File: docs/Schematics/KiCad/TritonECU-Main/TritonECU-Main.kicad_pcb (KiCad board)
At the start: 4 copper layers, 158 x 174 mm, 4 parts, among them J1 EEC-V 104

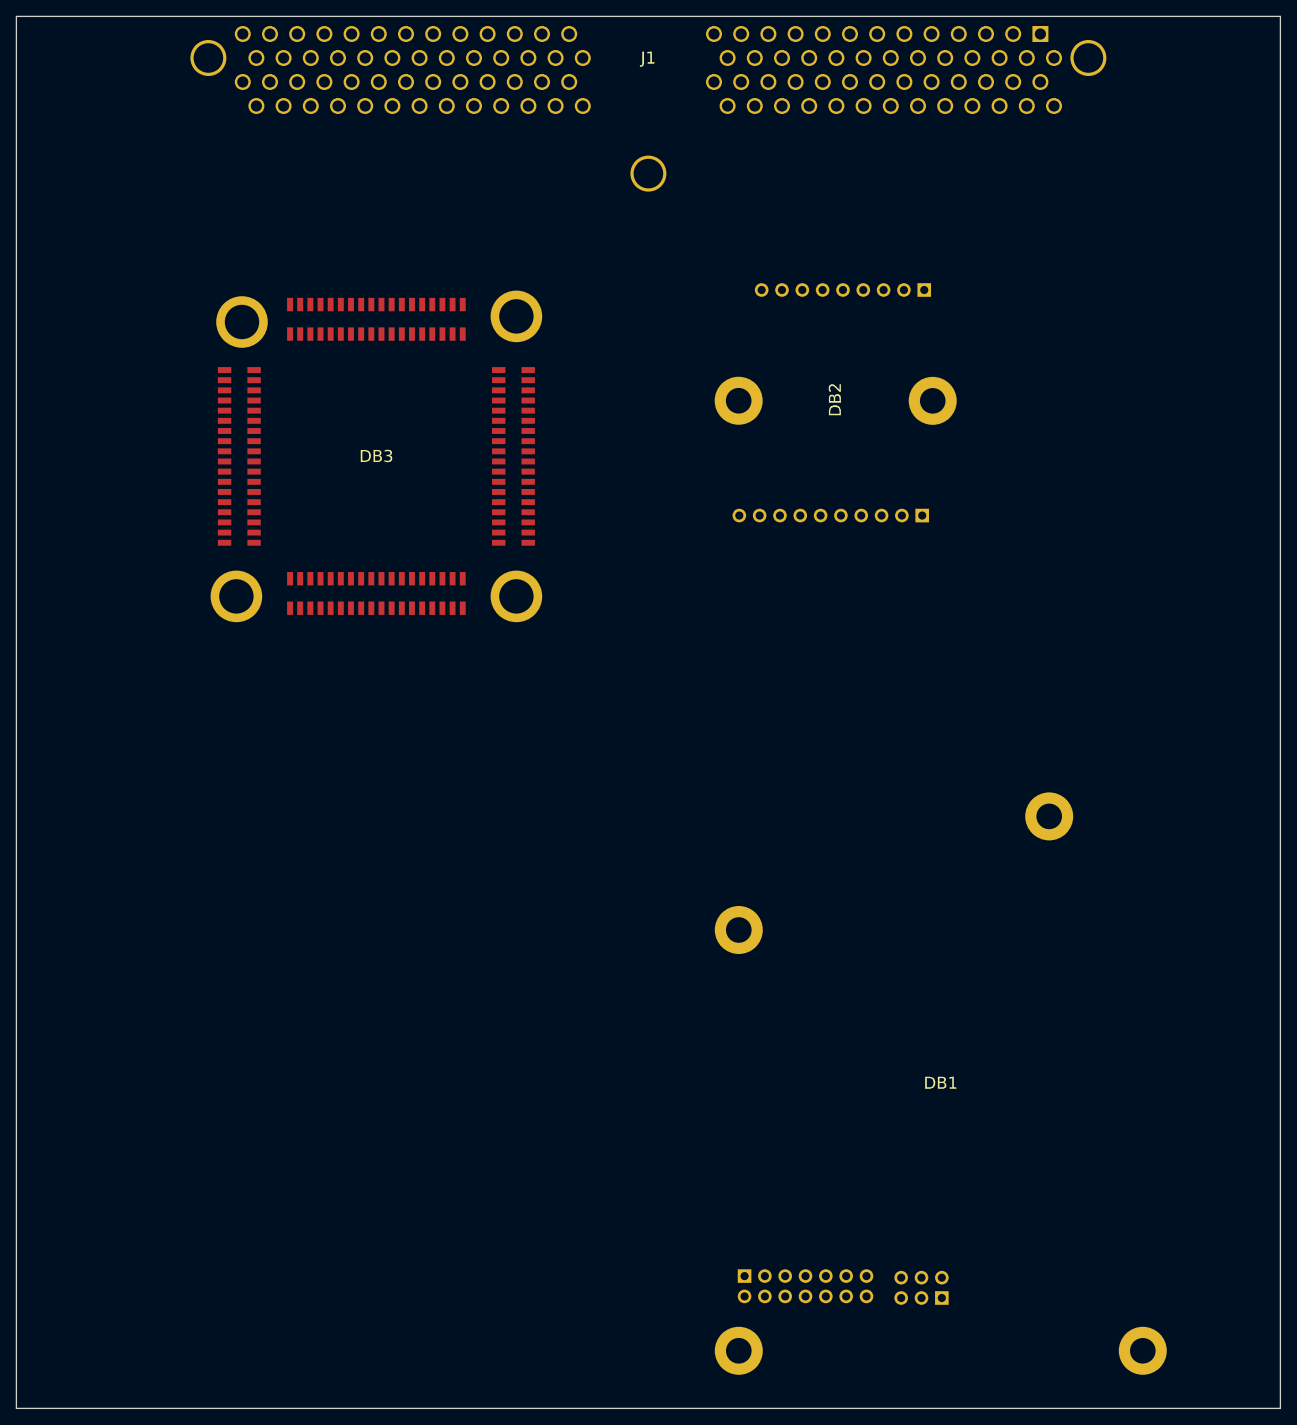
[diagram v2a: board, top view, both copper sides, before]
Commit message: Carrier: ignition, injection and rails sheets, placed on the main board
- eecv_pins.py: the EEC-V connector map for the 5.4L, checked. Corrects SSA/SSB
  to pins 6/11: Ford's "PCM 27 (*6)" legend is * = 5.4L, and 27/1 are coils 5/6
  on this truck (schematic-ecu-v1.txt and measurements-wanted.md fixed).
- carrier_pinmap.py: adds TCS (O/D cancel, pin 29) on PE1, polled; 4x4-low has
  no PCM pin in either source, marked [CONFIRM]. 100 signals, 5 spare.
- Interconnect sheet rebuilt every run with every connector and module pin
  labelled from the two maps (symbol UUIDs kept); deliberate no-connects flagged.
- gen_carrier.py: Rails, Ignition (74HCT541, 8x ISL9V3040, TPS3823A-33 watchdog
  on NRST and OE2 via BSS138, JP101 v1 strap) and Injection (8x ZXMS6005DGQ,
  10k input pulldowns). Deterministic symbol UUIDs keep the PCB linked. Own
  symbols for the IntelliFET (the Samacsys import is broken) and NCV8772.
- gen_carrier_pcb.py: adds missing parts to the board linked to their symbols,
  sets every pad net from the netlist, places a first-draft floor plan by
  connector position. DRC: no courtyard overlaps, schematic parity clean.
- ADC goes back on the carrier: adc-daughterboard.md superseded.

Co-Authored-By: Claude Opus 5.5 <noreply@anthropic.com>
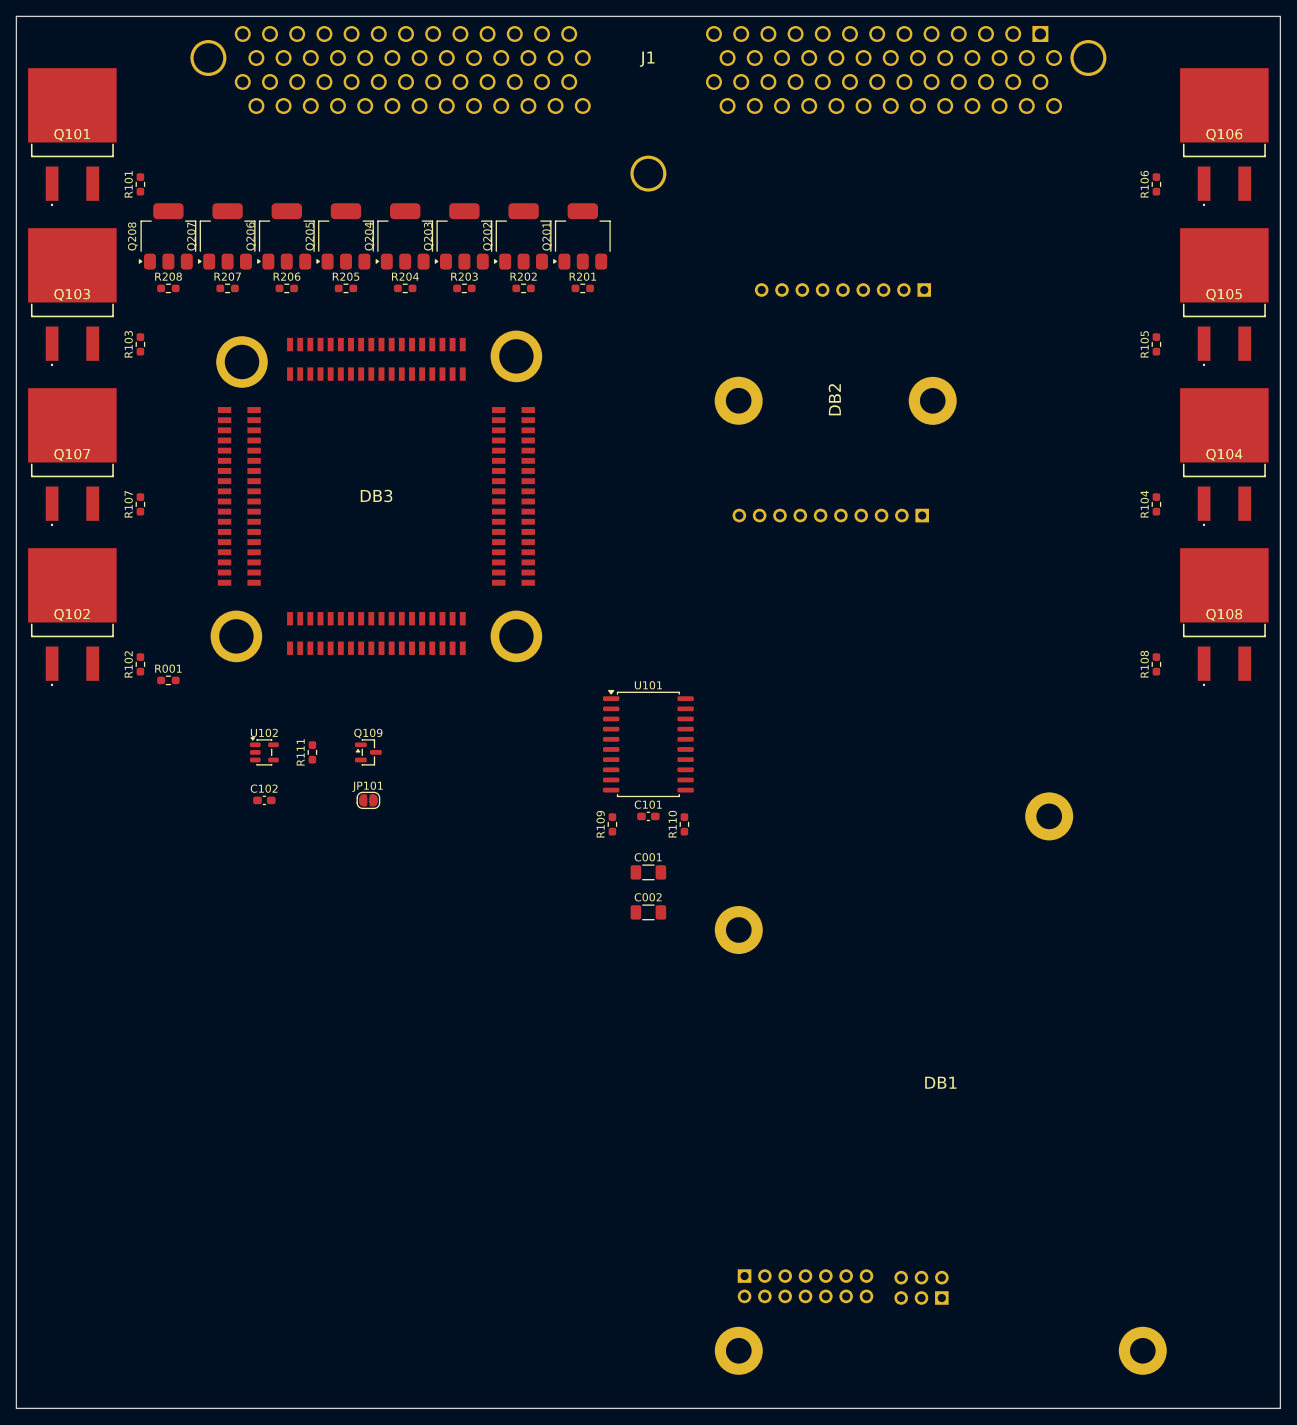
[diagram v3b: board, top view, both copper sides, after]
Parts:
- added C001: 10u, Capacitor_SMD:C_1206_3216Metric_Pad1.33x1.80mm_HandSolder, F.Cu at (104.0, 132.0)
- added C002: 10u, Capacitor_SMD:C_1206_3216Metric_Pad1.33x1.80mm_HandSolder, F.Cu at (104.0, 137.0)
- added C101: 100n, Capacitor_SMD:C_0603_1608Metric_Pad1.08x0.95mm_HandSolder, F.Cu at (104.0, 125.0)
- added C102: 100n, Capacitor_SMD:C_0603_1608Metric_Pad1.08x0.95mm_HandSolder, F.Cu at (56.0, 123.0)
- added JP101: OE2 strap, Jumper:SolderJumper-2_P1.3mm_Open_RoundedPad1.0x1.5mm, F.Cu at (69.0, 123.0)
- added Q101: ISL9V3040S3ST, Samacsys:ISL9V3040S3ST, F.Cu at (32.0, 38.0)
- added Q102: ISL9V3040S3ST, Samacsys:ISL9V3040S3ST, F.Cu at (32.0, 98.0)
- added Q103: ISL9V3040S3ST, Samacsys:ISL9V3040S3ST, F.Cu at (32.0, 58.0)
- added Q104: ISL9V3040S3ST, Samacsys:ISL9V3040S3ST, F.Cu at (176.0, 78.0)
- added Q105: ISL9V3040S3ST, Samacsys:ISL9V3040S3ST, F.Cu at (176.0, 58.0)
- added Q106: ISL9V3040S3ST, Samacsys:ISL9V3040S3ST, F.Cu at (176.0, 38.0)
- added Q107: ISL9V3040S3ST, Samacsys:ISL9V3040S3ST, F.Cu at (32.0, 78.0)
- added Q108: ISL9V3040S3ST, Samacsys:ISL9V3040S3ST, F.Cu at (176.0, 98.0)
- added Q109: BSS138, Package_TO_SOT_SMD:SOT-23, F.Cu at (69.0, 117.0)
- added Q201: ZXMS6005DGQTA, Package_TO_SOT_SMD:SOT-223-3_TabPin2, F.Cu at (95.8, 52.5)
- added Q202: ZXMS6005DGQTA, Package_TO_SOT_SMD:SOT-223-3_TabPin2, F.Cu at (88.4, 52.5)
- added Q203: ZXMS6005DGQTA, Package_TO_SOT_SMD:SOT-223-3_TabPin2, F.Cu at (81.0, 52.5)
- added Q204: ZXMS6005DGQTA, Package_TO_SOT_SMD:SOT-223-3_TabPin2, F.Cu at (73.6, 52.5)
- added Q205: ZXMS6005DGQTA, Package_TO_SOT_SMD:SOT-223-3_TabPin2, F.Cu at (66.2, 52.5)
- added Q206: ZXMS6005DGQTA, Package_TO_SOT_SMD:SOT-223-3_TabPin2, F.Cu at (58.8, 52.5)
- added Q207: ZXMS6005DGQTA, Package_TO_SOT_SMD:SOT-223-3_TabPin2, F.Cu at (51.4, 52.5)
- added Q208: ZXMS6005DGQTA, Package_TO_SOT_SMD:SOT-223-3_TabPin2, F.Cu at (44.0, 52.5)
- added R001: 0, Resistor_SMD:R_0603_1608Metric_Pad0.98x0.95mm_HandSolder, F.Cu at (44.0, 108.0)
- added R101: 470, Resistor_SMD:R_0603_1608Metric_Pad0.98x0.95mm_HandSolder, F.Cu at (40.5, 46.0)
- added R102: 470, Resistor_SMD:R_0603_1608Metric_Pad0.98x0.95mm_HandSolder, F.Cu at (40.5, 106.0)
- added R103: 470, Resistor_SMD:R_0603_1608Metric_Pad0.98x0.95mm_HandSolder, F.Cu at (40.5, 66.0)
- added R104: 470, Resistor_SMD:R_0603_1608Metric_Pad0.98x0.95mm_HandSolder, F.Cu at (167.5, 86.0)
- added R105: 470, Resistor_SMD:R_0603_1608Metric_Pad0.98x0.95mm_HandSolder, F.Cu at (167.5, 66.0)
- added R106: 470, Resistor_SMD:R_0603_1608Metric_Pad0.98x0.95mm_HandSolder, F.Cu at (167.5, 46.0)
- added R107: 470, Resistor_SMD:R_0603_1608Metric_Pad0.98x0.95mm_HandSolder, F.Cu at (40.5, 86.0)
- added R108: 470, Resistor_SMD:R_0603_1608Metric_Pad0.98x0.95mm_HandSolder, F.Cu at (167.5, 106.0)
- added R109: 10k, Resistor_SMD:R_0603_1608Metric_Pad0.98x0.95mm_HandSolder, F.Cu at (99.5, 126.0)
- added R110: 10k, Resistor_SMD:R_0603_1608Metric_Pad0.98x0.95mm_HandSolder, F.Cu at (108.5, 126.0)
- added R111: 1M, Resistor_SMD:R_0603_1608Metric_Pad0.98x0.95mm_HandSolder, F.Cu at (62.0, 117.0)
- added R201: 10k, Resistor_SMD:R_0603_1608Metric_Pad0.98x0.95mm_HandSolder, F.Cu at (95.8, 59.0)
- added R202: 10k, Resistor_SMD:R_0603_1608Metric_Pad0.98x0.95mm_HandSolder, F.Cu at (88.4, 59.0)
- added R203: 10k, Resistor_SMD:R_0603_1608Metric_Pad0.98x0.95mm_HandSolder, F.Cu at (81.0, 59.0)
- added R204: 10k, Resistor_SMD:R_0603_1608Metric_Pad0.98x0.95mm_HandSolder, F.Cu at (73.6, 59.0)
- added R205: 10k, Resistor_SMD:R_0603_1608Metric_Pad0.98x0.95mm_HandSolder, F.Cu at (66.2, 59.0)
- added R206: 10k, Resistor_SMD:R_0603_1608Metric_Pad0.98x0.95mm_HandSolder, F.Cu at (58.8, 59.0)
- added R207: 10k, Resistor_SMD:R_0603_1608Metric_Pad0.98x0.95mm_HandSolder, F.Cu at (51.4, 59.0)
- added R208: 10k, Resistor_SMD:R_0603_1608Metric_Pad0.98x0.95mm_HandSolder, F.Cu at (44.0, 59.0)
- added U101: 74HCT541, Package_SO:SOIC-20W_7.5x12.8mm_P1.27mm, F.Cu at (104.0, 116.0)
- added U102: TPS3823A-33DBVR, Package_TO_SOT_SMD:SOT-23-5, F.Cu at (56.0, 117.0)
- moved DB3 5.00 mm to (70.0, 85.0)
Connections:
- DB1 pad A10: SDA -> I2C_SDA
- DB1 pad A12: 3.3_ENOUT -> ENOUT
- DB1 pad A6: SCL -> I2C_SCL
- DB1 pad A9: 3_GOOD -> unconnected-(DB1-3_GOOD-PadA9)
- DB1 pad B1: +5V -> GND
- DB1 pad B3: +VIN -> VPWR
- DB1 pad B4: +VIN -> VPWR
- DB3 pad A10: unconnected-(DB3-PC13-PadA10) -> IGN_WAKE
- DB3 pad A11: unconnected-(DB3-PF0-PadA11) -> I2C_SDA
- DB3 pad A12: unconnected-(DB3-PF1-PadA12) -> I2C_SCL
- DB3 pad A13: unconnected-(DB3-PF2-PadA13) -> U_SHDN
- DB3 pad A14: unconnected-(DB3-PF3-PadA14) -> DPFE
- DB3 pad A15: unconnected-(DB3-PF4-PadA15) -> TFT
- DB3 pad A16: unconnected-(DB3-PF5-PadA16) -> VIN_ALERT
- DB3 pad A19: unconnected-(DB3-PF6-PadA19) -> O2_DN1
- DB3 pad A20: unconnected-(DB3-PF7-PadA20) -> O2_DN2
- DB3 pad A21: unconnected-(DB3-PF8-PadA21) -> IAC
- DB3 pad A22: unconnected-(DB3-PF9-PadA22) -> VREF_FAULT
- DB3 pad A23: unconnected-(DB3-PF10-PadA23) -> FP_MON
- DB3 pad A24: unconnected-(DB3-NRST-PadA24) -> NRST
- DB3 pad A25: unconnected-(DB3-PC0-PadA25) -> TR3A
- DB3 pad A26: unconnected-(DB3-PC1-PadA26) -> VREF_CS
- DB3 pad A27: unconnected-(DB3-PC2-PadA27) -> VREF_STB
- DB3 pad A28: unconnected-(DB3-PC3-PadA28) -> KNOCK
- DB3 pad A31: unconnected-(DB3-PA0-PadA31) -> CAN_RX_WAKE
- DB3 pad A32: unconnected-(DB3-PA1-PadA32) -> J1850_RX
- DB3 pad A33: unconnected-(DB3-PA2-PadA33) -> MUX_OUT
- DB3 pad A4: unconnected-(DB3-PE2-PadA4) -> ENOUT
- DB3 pad A5: unconnected-(DB3-PE3-PadA5) -> M_SYNC
- DB3 pad A6: unconnected-(DB3-PE4-PadA6) -> FLT
- DB3 pad A7: unconnected-(DB3-PE5-PadA7) -> EVAP
- DB3 pad A8: unconnected-(DB3-PE6-PadA8) -> EGR
- DB3 pad A9: unconnected-(DB3-VBAT-PadA9) -> VBAT
- DB3 pad B10: unconnected-(DB3-PC5-PadB10) -> VREF_SEL
- DB3 pad B11: unconnected-(DB3-PB0-PadB11) -> MUX_S0
- DB3 pad B12: unconnected-(DB3-PB1-PadB12) -> MUX_S1
- DB3 pad B13: unconnected-(DB3-PB2-PadB13) -> VREF_EN
- DB3 pad B14: unconnected-(DB3-PF11-PadB14) -> TR1
- DB3 pad B15: unconnected-(DB3-PF12-PadB15) -> TR2
- DB3 pad B18: unconnected-(DB3-PF13-PadB18) -> VREF_IN1
- DB3 pad B19: unconnected-(DB3-PF14-PadB19) -> TR4
- DB3 pad B2: unconnected-(DB3-PA3-PadB2) -> VSS_OUT
- DB3 pad B20: unconnected-(DB3-PF15-PadB20) -> BRAKE
- DB3 pad B21: unconnected-(DB3-PG0-PadB21) -> ACC
- DB3 pad B22: unconnected-(DB3-PG1-PadB22) -> 5_GOOD
- DB3 pad B23: unconnected-(DB3-PE7-PadB23) -> FPUMP
- DB3 pad B24: unconnected-(DB3-PE8-PadB24) -> 4X4L
- DB3 pad B25: unconnected-(DB3-PE9-PadB25) -> INJ1
- DB3 pad B28: unconnected-(DB3-PE10-PadB28) -> ACP
- DB3 pad B29: unconnected-(DB3-PE11-PadB29) -> INJ2
- DB3 pad B30: unconnected-(DB3-PE12-PadB30) -> FAN1
- DB3 pad B31: unconnected-(DB3-PE13-PadB31) -> INJ3
- DB3 pad B32: unconnected-(DB3-PE14-PadB32) -> INJ4
- DB3 pad B33: unconnected-(DB3-PE15-PadB33) -> FAN2
- DB3 pad B34: unconnected-(DB3-PB10-PadB34) -> CMP
- DB3 pad B35: unconnected-(DB3-PB11-PadB35) -> ADC_CONVST
- DB3 pad B5: unconnected-(DB3-PA4-PadB5) -> O2_BIAS
- DB3 pad B6: unconnected-(DB3-PA5-PadB6) -> TACH
- DB3 pad B7: unconnected-(DB3-PA6-PadB7) -> SPEED
- DB3 pad B8: unconnected-(DB3-PA7-PadB8) -> MUX_S2
- DB3 pad B9: unconnected-(DB3-PC4-PadB9) -> VREF_IN2
- DB3 pad C10: unconnected-(DB3-PD12-PadC10) -> COIL1
- DB3 pad C11: unconnected-(DB3-PD13-PadC11) -> COIL2
- DB3 pad C14: unconnected-(DB3-PD14-PadC14) -> COIL3
- DB3 pad C15: unconnected-(DB3-PD15-PadC15) -> COIL4
- DB3 pad C16: unconnected-(DB3-PG2-PadC16) -> HTR11
- DB3 pad C17: unconnected-(DB3-PG3-PadC17) -> HTR21
- DB3 pad C18: unconnected-(DB3-PG4-PadC18) -> HTR12
- DB3 pad C19: unconnected-(DB3-PG5-PadC19) -> HTR22
- DB3 pad C2: unconnected-(DB3-PB12-PadC2) -> SSB
- DB3 pad C20: unconnected-(DB3-PG6-PadC20) -> VENT
- DB3 pad C21: unconnected-(DB3-PG7-PadC21) -> IMCC
- DB3 pad C22: unconnected-(DB3-PG8-PadC22) -> SSA
- DB3 pad C25: unconnected-(DB3-PC6-PadC25) -> COIL5
- DB3 pad C26: unconnected-(DB3-PC7-PadC26) -> COIL6
- DB3 pad C27: unconnected-(DB3-PC8-PadC27) -> COIL7
- DB3 pad C28: unconnected-(DB3-PC9-PadC28) -> COIL8
- DB3 pad C29: unconnected-(DB3-PA8-PadC29) -> PWM_OE
- DB3 pad C3: unconnected-(DB3-PB13-PadC3) -> CCS
- DB3 pad C30: unconnected-(DB3-PA9-PadC30) -> USB_VBUS
- DB3 pad C32: unconnected-(DB3-PA11-PadC32) -> USB_DM
- DB3 pad C33: unconnected-(DB3-PA12-PadC33) -> USB_DP
- DB3 pad C4: unconnected-(DB3-PB14-PadC4) -> INJ7
- DB3 pad C5: unconnected-(DB3-PB15-PadC5) -> INJ8
- DB3 pad C8: unconnected-(DB3-PD10-PadC8) -> WDI
- DB3 pad C9: unconnected-(DB3-PD11-PadC9) -> COIL_ARM
- DB3 pad D10: unconnected-(DB3-PD3-PadD10) -> ADC_BUSY
- DB3 pad D11: unconnected-(DB3-PD4-PadD11) -> ADC_RESET
- DB3 pad D12: unconnected-(DB3-PD5-PadD12) -> CAN_STB
- DB3 pad D15: unconnected-(DB3-PD6-PadD15) -> SD_CK
- DB3 pad D16: unconnected-(DB3-PD7-PadD16) -> SD_CMD
- DB3 pad D17: unconnected-(DB3-PG9-PadD17) -> SD_D0
- DB3 pad D21: unconnected-(DB3-PG13-PadD21) -> J1850_TXP
- DB3 pad D22: unconnected-(DB3-PG14-PadD22) -> J1850_TXN
- DB3 pad D25: unconnected-(DB3-PG15-PadD25) -> J1850_NSLEEP
- DB3 pad D27: unconnected-(DB3-PB4-PadD27) -> INJ5
- DB3 pad D28: unconnected-(DB3-PB5-PadD28) -> INJ6
- DB3 pad D29: unconnected-(DB3-PB6-PadD29) -> OSS
- DB3 pad D3: unconnected-(DB3-PA15-PadD3) -> CKP
- DB3 pad D30: unconnected-(DB3-PB7-PadD30) -> TSS
- DB3 pad D31: unconnected-(DB3-BOOT0-PadD31) -> BOOT0
- DB3 pad D32: unconnected-(DB3-PB8-PadD32) -> EPC
- DB3 pad D33: unconnected-(DB3-PB9-PadD33) -> TCC
- DB3 pad D34: unconnected-(DB3-PE0-PadD34) -> TC_SPEED
- DB3 pad D35: unconnected-(DB3-PE1-PadD35) -> TCS
- DB3 pad D4: unconnected-(DB3-PC10-PadD4) -> ADC_SCK
- DB3 pad D5: unconnected-(DB3-PC11-PadD5) -> ADC_MISO
- DB3 pad D7: unconnected-(DB3-PD0-PadD7) -> CAN_RX
- DB3 pad D8: unconnected-(DB3-PD1-PadD8) -> CAN_TX
- DB3 pad D9: unconnected-(DB3-PD2-PadD9) -> ADC_CS
- J1 pad 1: unconnected-(J1-Ign_Coil_6-Pad1) -> COIL6_OUT
- J1 pad 100: unconnected-(J1-Injector_4-Pad100) -> INJ4_OUT
- J1 pad 101: unconnected-(J1-Injector_2-Pad101) -> INJ2_OUT
- J1 pad 103: unconnected-(J1-GND-Pad103) -> GND
- J1 pad 104: unconnected-(J1-IGN_Coil_2-Pad104) -> COIL2_OUT
- J1 pad 11: unconnected-(J1-Shift_SOL(SS2)-Pad11) -> SSB_OUT
- J1 pad 15: unconnected-(J1-SCP--Pad15) -> SCP_N
- J1 pad 16: unconnected-(J1-SCP+-Pad16) -> SCP_P
- J1 pad 18: unconnected-(J1-Pad18) -> FAN2_OUT
- J1 pad 19: unconnected-(J1-Pad19) -> FAN1_OUT
- J1 pad 20: unconnected-(J1-CSS_FREE-Pad20) -> CCS_OUT
- J1 pad 21: unconnected-(J1-CKP+-Pad21) -> CKP_P
- J1 pad 22: unconnected-(J1-CKP--Pad22) -> CKP_N
- J1 pad 25: unconnected-(J1-CMP_shield_drain-Pad25) -> CMP_SHIELD
- J1 pad 26: unconnected-(J1-Ign_Coil_1-Pad26) -> COIL1_OUT
- J1 pad 27: unconnected-(J1-Ign_Coil_5-Pad27) -> COIL5_OUT
- J1 pad 29: unconnected-(J1-TCS-Pad29) -> TCS_IN
- J1 pad 3: unconnected-(J1-GND-Pad3) -> GND
- J1 pad 32: unconnected-(J1-KS_Sensor-Pad32) -> KNOCK_RTN
- J1 pad 34: unconnected-(J1-Trans_Pos_Sensor_1-Pad34) -> TR1_IN
- J1 pad 35: unconnected-(J1-RR_HO2S_Signal-Pad35) -> O2_12_IN
- J1 pad 36: unconnected-(J1-MAF_Return-Pad36) -> MAF_RTN
- J1 pad 37: unconnected-(J1-TFT-Pad37) -> TFT_IN
- J1 pad 39: unconnected-(J1-IAT-Pad39) -> IAT_IN
- J1 pad 40: unconnected-(J1-Fuel_Pump_Monitor-Pad40) -> FP_MON_IN
- J1 pad 41: unconnected-(J1-A/C_cycle_Sw-Pad41) -> ACP_IN
- J1 pad 46: unconnected-(J1-Intake_Manifold_Communicator(I-Pad46) -> IMCC_OUT
- J1 pad 47: unconnected-(J1-EVR_CTRL-Pad47) -> EGR_OUT
- J1 pad 48: unconnected-(J1-Pad48) -> FW_391
- J1 pad 49: unconnected-(J1-Trans_Pos_Sensor_2-Pad49) -> TR2_IN
- J1 pad 50: unconnected-(J1-Trans_Pos_Sensor_4-Pad50) -> TR4_IN
- J1 pad 51: unconnected-(J1-GND-Pad51) -> GND
- J1 pad 52: unconnected-(J1-Ign_Coil_3-Pad52) -> COIL3_OUT
- J1 pad 53: unconnected-(J1-Ign_Coil_4-Pad53) -> COIL4_OUT
- J1 pad 54: unconnected-(J1-TCC_SOL-Pad54) -> TCC_OUT
- J1 pad 55: unconnected-(J1-B+_KAM-Pad55) -> VBAT_SENSE
- J1 pad 56: unconnected-(J1-VAPOR_VALVE-Pad56) -> EVAP_OUT
- J1 pad 57: unconnected-(J1-KNOCK_SENSOR-Pad57) -> KNOCK_IN
- J1 pad 59: unconnected-(J1-TSS_Speed_Sensor-Pad59) -> TSS_IN
- J1 pad 6: unconnected-(J1-Shift_SOL(SS1)-Pad6) -> SSA_OUT
- J1 pad 60: unconnected-(J1-RF_O2-Pad60) -> O2_11_IN
- J1 pad 61: unconnected-(J1-LR_HO2S_Signal-Pad61) -> O2_22_IN
- J1 pad 64: unconnected-(J1-Trans_Pos_Sensor_3_(TR3A)__and-Pad64) -> TR3A_IN
- J1 pad 65: unconnected-(J1-DPFE_Sensor-Pad65) -> DPFE_IN
- J1 pad 66: unconnected-(J1-CYL_Head_Temp-Pad66) -> CHT_IN
- J1 pad 67: unconnected-(J1-Canister_Vent-Pad67) -> VENT_OUT
- J1 pad 68: unconnected-(J1-VSS+-Pad68) -> VSS_OUT_PIN
- J1 pad 69: unconnected-(J1-AC_WOT_Clutch-Pad69) -> ACC_OUT
- J1 pad 7: unconnected-(J1-TC_Speed_Sense-Pad7) -> TC_SPEED_IN
- J1 pad 71: unconnected-(J1-12V_Switched-Pad71) -> VPWR
- J1 pad 72: unconnected-(J1-Injector_7-Pad72) -> INJ7_OUT
- J1 pad 73: unconnected-(J1-Injector_5-Pad73) -> INJ5_OUT
- J1 pad 74: unconnected-(J1-Injector_3-Pad74) -> INJ3_OUT
- J1 pad 75: unconnected-(J1-Injector_1-Pad75) -> INJ1_OUT
- J1 pad 77: unconnected-(J1-GND-Pad77) -> GND
- J1 pad 78: unconnected-(J1-Ign_Coil_7-Pad78) -> COIL7_OUT
- J1 pad 79: unconnected-(J1-Ign_Coil_8-Pad79) -> COIL8_OUT
- J1 pad 80: unconnected-(J1-FP-Pad80) -> FPUMP_OUT
- J1 pad 81: unconnected-(J1-EPC_SOL-Pad81) -> EPC_OUT
- J1 pad 82: unconnected-(J1-Pad82) -> FW_1138
- J1 pad 83: unconnected-(J1-IAC-Pad83) -> IAC_OUT
- J1 pad 84: unconnected-(J1-OSS-Pad84) -> OSS_IN
- J1 pad 85: unconnected-(J1-CMP-Pad85) -> CMP_IN
- J1 pad 87: unconnected-(J1-LF_O2-Pad87) -> O2_21_IN
- J1 pad 88: unconnected-(J1-MAF-Pad88) -> MAF_IN
- J1 pad 89: unconnected-(J1-TPS-Pad89) -> TPS_IN
- J1 pad 90: unconnected-(J1-VREF-Pad90) -> VREF
- J1 pad 91: unconnected-(J1-SGND-Pad91) -> SIGRTN
- J1 pad 92: unconnected-(J1-BPP_SW-Pad92) -> BRAKE_IN
- J1 pad 93: unconnected-(J1-RF_O2_Heat-Pad93) -> HTR11_OUT
- J1 pad 94: unconnected-(J1-LF_O2_Heat-Pad94) -> HTR21_OUT
- J1 pad 95: unconnected-(J1-RR_HO2S_Heat-Pad95) -> HTR12_OUT
- J1 pad 96: unconnected-(J1-LR_HO2S_Heat-Pad96) -> HTR22_OUT
- J1 pad 97: unconnected-(J1-12V_Switched-Pad97) -> VPWR
- J1 pad 98: unconnected-(J1-Injector_8-Pad98) -> INJ8_OUT
- J1 pad 99: unconnected-(J1-Injector_6-Pad99) -> INJ6_OUT
